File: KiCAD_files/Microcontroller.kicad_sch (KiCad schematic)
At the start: 58 parts, among them J403 RJE721881411, J404 RJE721881411, U401 OwnTech_SPIN, U402 TCAN334GDR, U405 LTC2850xS8, U406 MCP6487T-E/SN

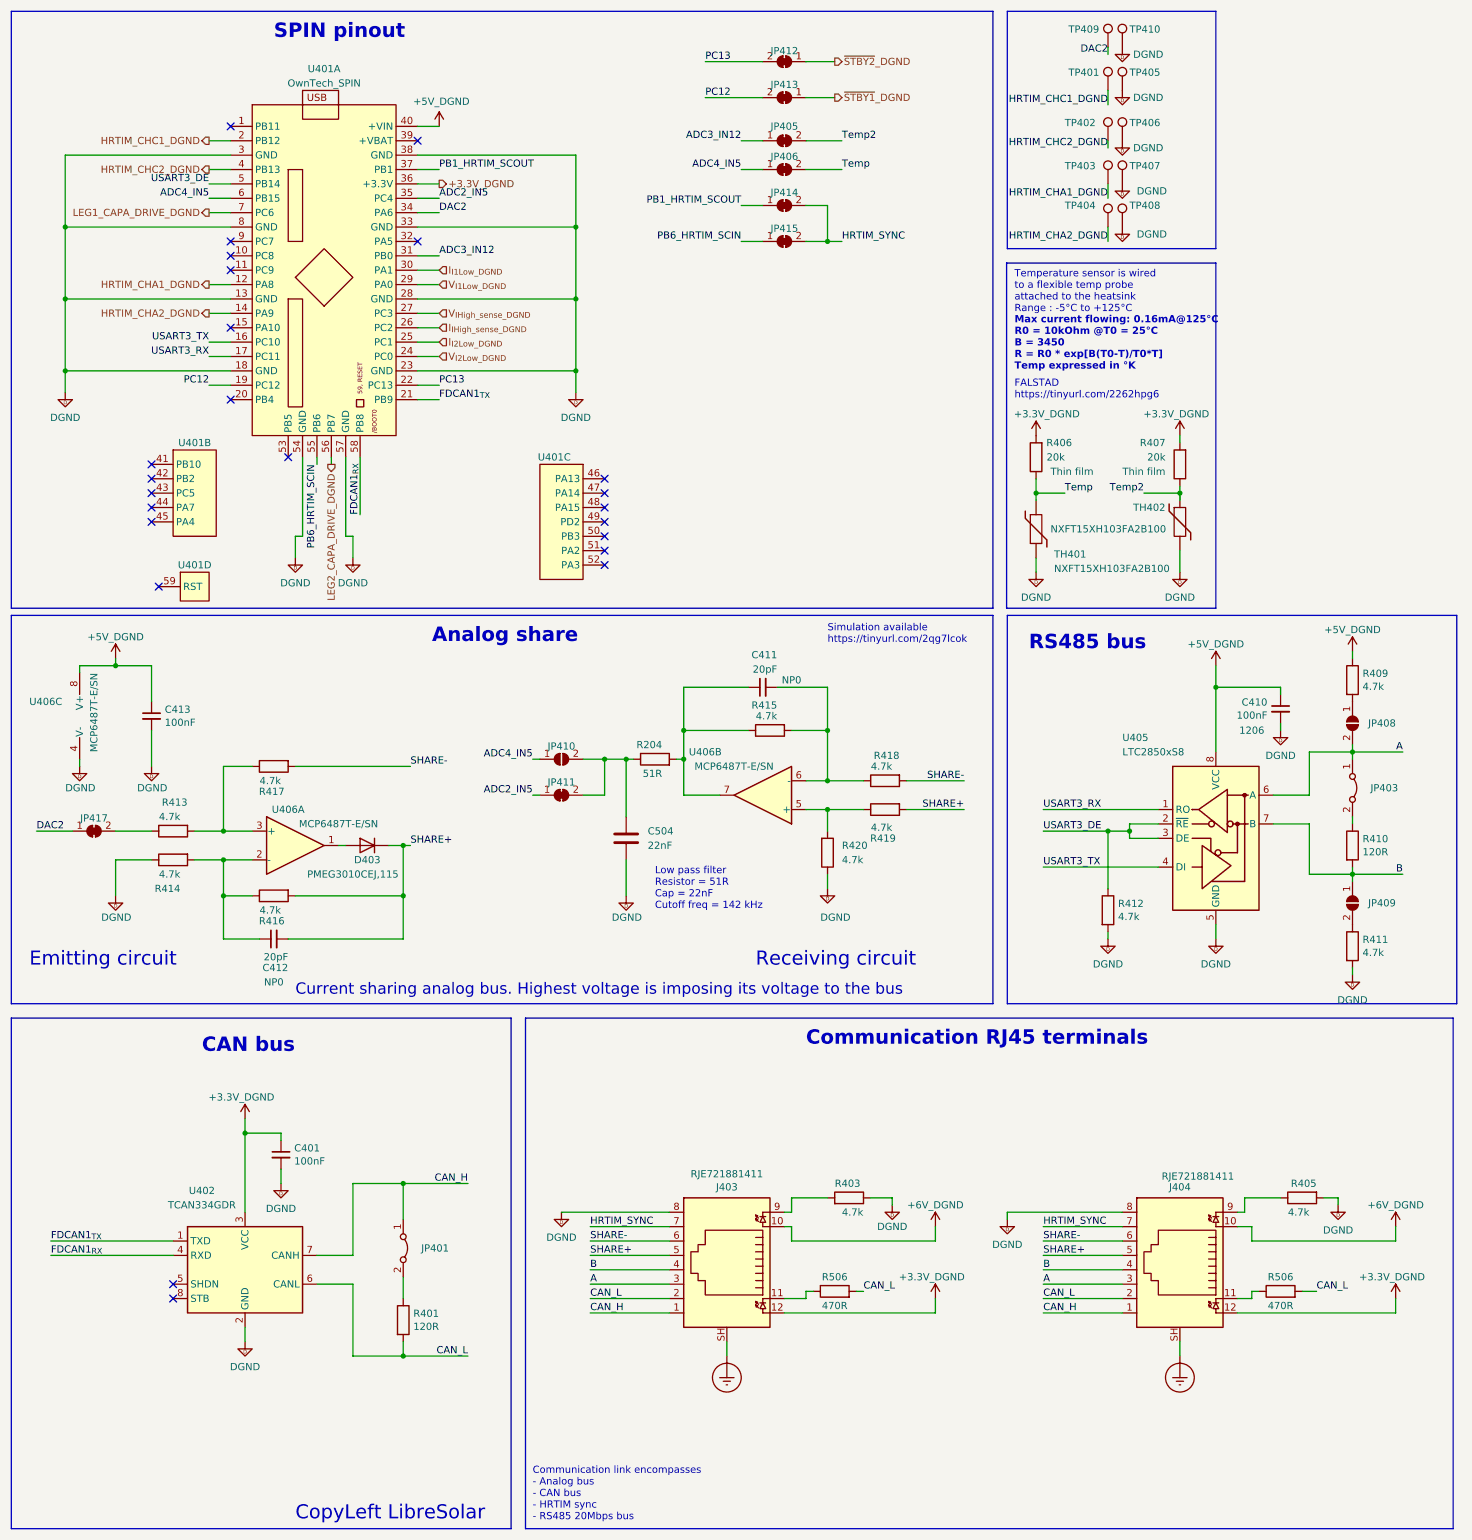
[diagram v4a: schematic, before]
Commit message: Major change - FDCAN1 -> FDCAN2 in order to remove conflit on pin PB8 BOOT0
FDCAN1Rx pin PB8 -> FDCAN2Rx pin PB5
FDCAN1Tx pin PB9 -> FDCAN2Tx pin PB6
HRTIM1_SCIN pin PB6 -> HRTIM1_SCIN pin PB2.

Signed-off-by: Jean Alinei <jean.alinei@laas.fr>
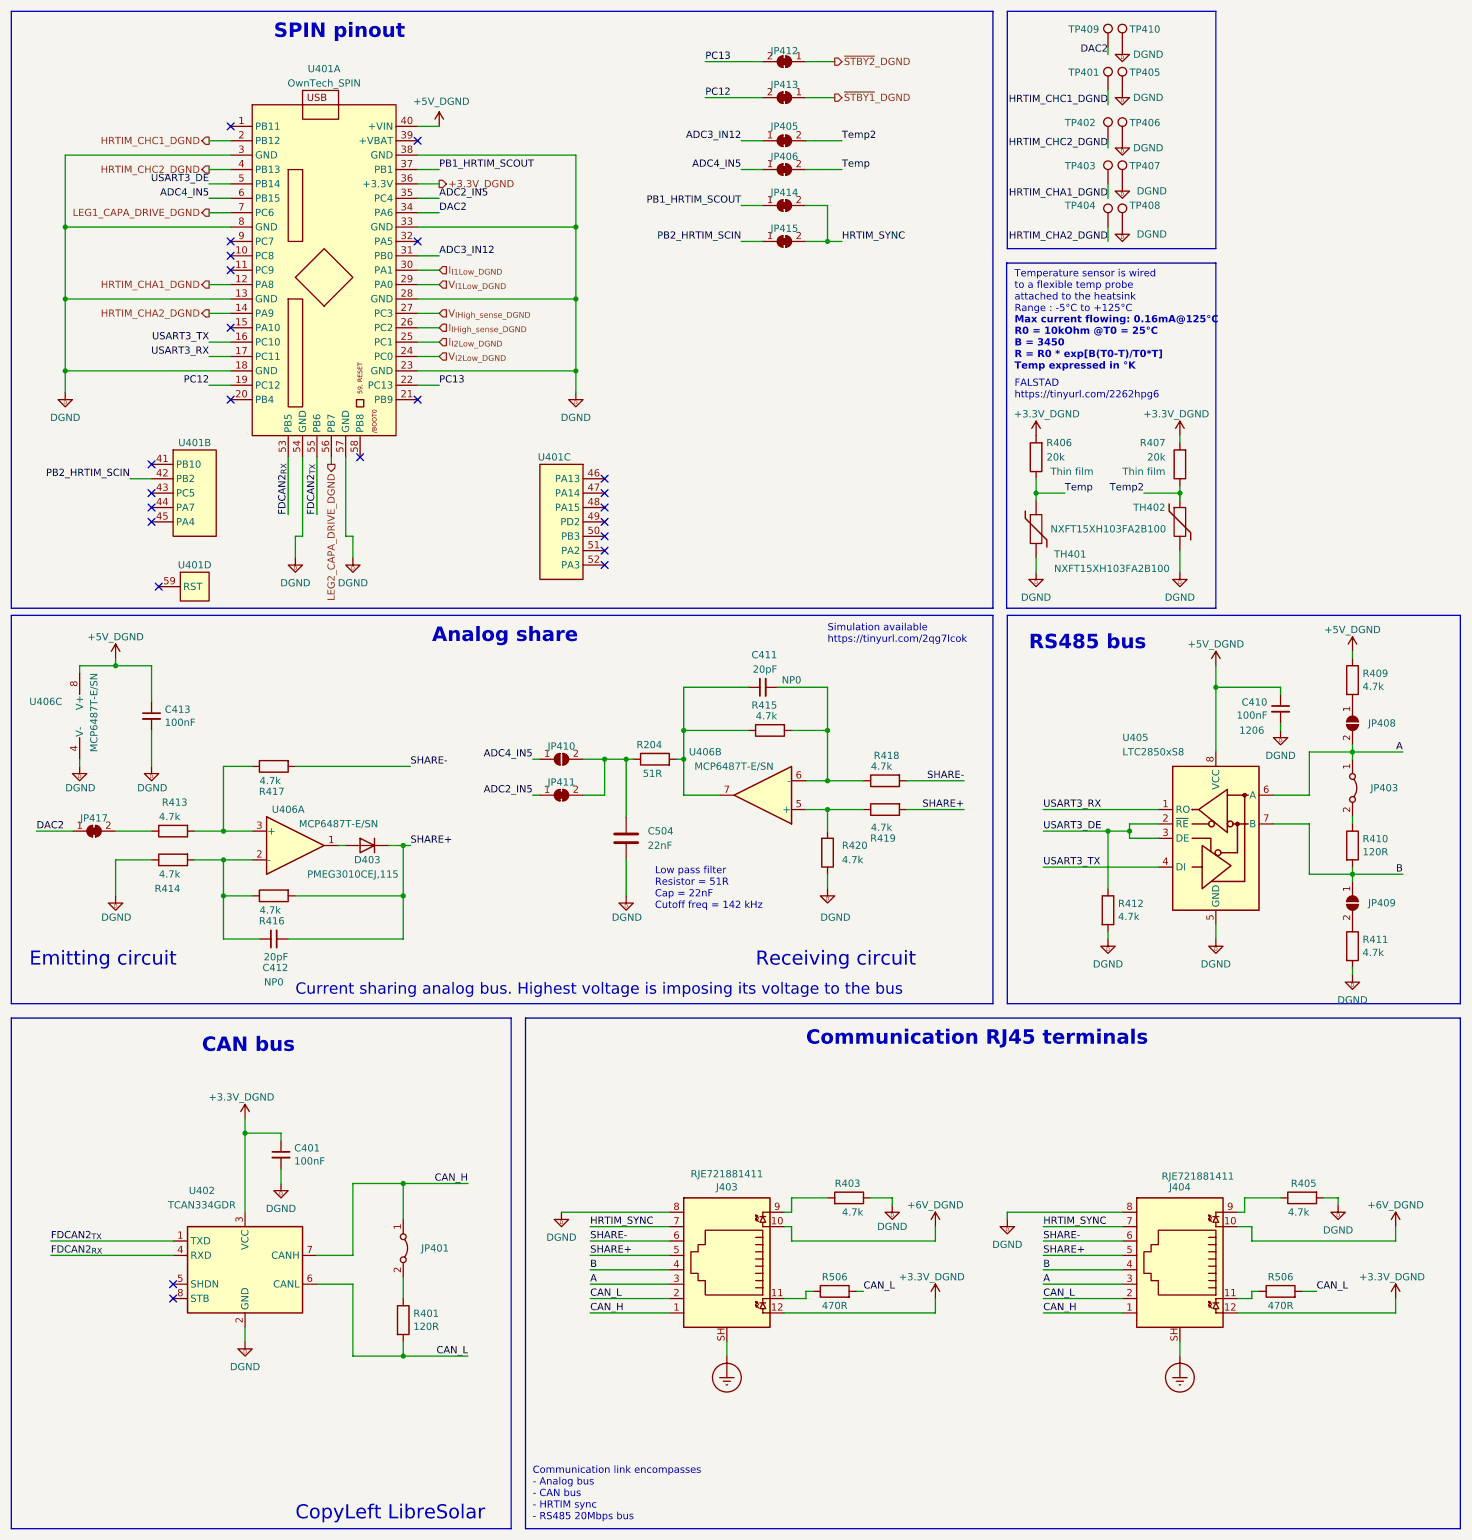
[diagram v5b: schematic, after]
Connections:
- net FDCAN2_{RX}: now reaches U401.53 (PB5)
- net FDCAN2_{RX}: now also U402.4 (RXD)
- net PB2_HRTIM_SCIN: now reaches U401.42 (PB2)
- net PB2_HRTIM_SCIN: now also JP415.1 (A)
- net FDCAN1_{RX}: no longer names the net of U401.58 (PB8)
- net FDCAN1_{RX}: no longer U402.4 (RXD)
- net FDCAN1_{TX}: no longer names the net of U401.21 (PB9)
- net FDCAN1_{TX}: no longer U402.1 (TXD)
- net PB6_HRTIM_SCIN renamed FDCAN2_{TX}
- net FDCAN2_{TX}: now also U402.1 (TXD); no longer JP415.1 (A)
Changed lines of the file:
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@@
   (junction (at 233.68 99.06) (diameter 0) (color 0 0 0 0)
   )
+  (no_connect (at 99.06 82.55))
   (no_connect (at 55.88 238.76))
   (no_connect (at 66.04 59.69))
@@
   (no_connect (at 55.88 241.3))
   (no_connect (at 66.04 82.55))
-  (no_connect (at 76.2 92.71))
   (no_connect (at 52.07 99.06))
   (no_connect (at 52.07 93.98))
-  (no_connect (at 52.07 96.52))
   (no_connect (at 132.08 101.6))
   (no_connect (at 132.08 104.14))
@@
   (no_connect (at 66.04 57.15))
   (no_connect (at 66.04 34.29))
+  (no_connect (at 88.9 92.71))
   (no_connect (at 53.34 115.57))
   (no_connect (at 132.08 111.76))
@@
     (stroke (width 0) (type default))
   )
+  (wire (pts (xy 76.2 92.71) (xy 76.2 102.87))
+    (stroke (width 0) (type default))
+  )
   (wire (pts (xy 52.07 129.54) (xy 45.72 129.54))
     (stroke (width 0) (type default))
@@
     (stroke (width 0) (type default))
   )
-  (wire (pts (xy 81.28 92.71) (xy 81.28 93.98))
-    (stroke (width 0) (type default))
-  )
   (wire (pts (xy 245.11 223.52) (xy 251.46 223.52))
     (stroke (width 0) (type default))
@@
     (stroke (width 0) (type default))
   )
-  (wire (pts (xy 88.9 92.71) (xy 88.9 102.87))
-    (stroke (width 0) (type default))
-  )
   (wire (pts (xy 31.75 158.75) (xy 38.1 158.75))
     (stroke (width 0) (type default))
@@
     (stroke (width 0) (type default))
   )
-  (wire (pts (xy 99.06 82.55) (xy 102.87 82.55))
-    (stroke (width 0) (type default))
-  )
   (wire (pts (xy 132.08 146.05) (xy 132.08 152.4))
     (stroke (width 0) (type default))
@@
     (stroke (width 0) (type default))
   )
+  (wire (pts (xy 48.26 96.52) (xy 52.07 96.52))
+    (stroke (width 0) (type default))
+  )
   (wire (pts (xy 233.68 99.06) (xy 233.68 100.33))
     (stroke (width 0) (type default))
@@
     (stroke (width 0) (type default))
   )
+  (wire (pts (xy 81.28 92.71) (xy 81.28 102.87))
+    (stroke (width 0) (type default))
+  )
   (wire (pts (xy 77.47 106.68) (xy 77.47 110.49))
     (stroke (width 0) (type default))
@@
     (fill (type none))
   )
-  (rectangle (start 203.2 120.65) (end 282.575 189.23)
+  (rectangle (start 203.2 120.65) (end 283.21 189.23)
     (stroke (width 0) (type default))
     (fill (type none))
@@
     (fill (type none))
   )
-  (rectangle (start 118.11 191.77) (end 281.94 281.94)
+  (rectangle (start 118.11 191.77) (end 283.21 281.94)
     (stroke (width 0) (type default))
     (fill (type none))
@@
     (effects (font (size 1.27 1.27)) (justify left bottom))
   )
+  (label "FDCAN2_{RX}" (at 76.2 102.87 90) (fields_autoplaced)
+    (effects (font (size 1.27 1.27)) (justify left bottom))
+  )
   (label "PC12" (at 149.86 29.21 0) (fields_autoplaced)
     (effects (font (size 1.27 1.27)) (justify left bottom))
@@
     (effects (font (size 1.27 1.27)) (justify right bottom))
   )
+  (label "FDCAN2_{TX}" (at 81.28 102.87 90) (fields_autoplaced)
+    (effects (font (size 1.27 1.27)) (justify left bottom))
+  )
   (label "ADC4_IN5" (at 62.23 46.99 180) (fields_autoplaced)
     (effects (font (size 1.27 1.27)) (justify right bottom))
   )
+  (label "PB2_HRTIM_SCIN" (at 48.26 96.52 180) (fields_autoplaced)
+    (effects (font (size 1.27 1.27)) (justify right bottom))
+  )
   (label "Temp2" (at 227.33 99.06 180) (fields_autoplaced)
     (effects (font (size 1.27 1.27)) (justify right bottom))
@@
     (effects (font (size 1.27 1.27)) (justify right bottom))
   )
-  (label "PB6_HRTIM_SCIN" (at 81.28 93.98 270) (fields_autoplaced)
-    (effects (font (size 1.27 1.27)) (justify right bottom))
-  )
   (label "SHARE+" (at 129.54 233.68 0) (fields_autoplaced)
     (effects (font (size 1.27 1.27)) (justify left bottom))
@@
     (effects (font (size 1.27 1.27)) (justify left bottom))
   )
-  (label "FDCAN1_{TX}" (at 34.29 231.14 0) (fields_autoplaced)
+  (label "FDCAN2_{TX}" (at 34.29 231.14 0) (fields_autoplaced)
     (effects (font (size 1.27 1.27)) (justify left bottom))
   )
@@
     (effects (font (size 1.27 1.27)) (justify left bottom))
   )
-  (label "PB6_HRTIM_SCIN" (at 156.21 54.61 180) (fields_autoplaced)
+  (label "PB2_HRTIM_SCIN" (at 156.21 54.61 180) (fields_autoplaced)
     (effects (font (size 1.27 1.27)) (justify right bottom))
   )
@@
     (effects (font (size 1.27 1.27)) (justify left bottom))
   )
-  (label "FDCAN1_{TX}" (at 102.87 82.55 0) (fields_autoplaced)
-    (effects (font (size 1.27 1.27)) (justify left bottom))
-  )
-  (label "FDCAN1_{RX}" (at 34.29 233.68 0) (fields_autoplaced)
+  (label "FDCAN2_{RX}" (at 34.29 233.68 0) (fields_autoplaced)
     (effects (font (size 1.27 1.27)) (justify left bottom))
   )
@@
     (effects (font (size 1.27 1.27)) (justify left bottom))
   )
-  (label "FDCAN1_{RX}" (at 88.9 102.87 90) (fields_autoplaced)
-    (effects (font (size 1.27 1.27)) (justify left bottom))
-  )

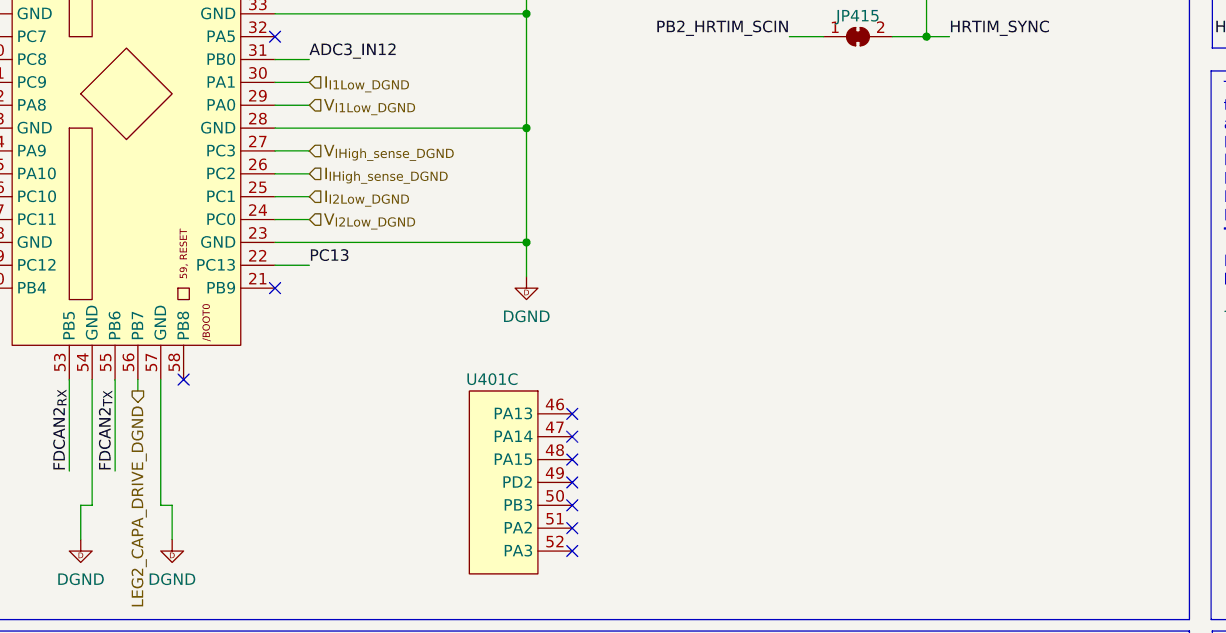
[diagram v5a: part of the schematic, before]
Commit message: Changed the silkscreen to math new CAN pinout - Improved DCDC ground contact Added few missing thermal reliefs - Added few exclusion zones between capacitor terminals
Signed-off-by: Jean Alinei <jean.alinei@laas.fr>
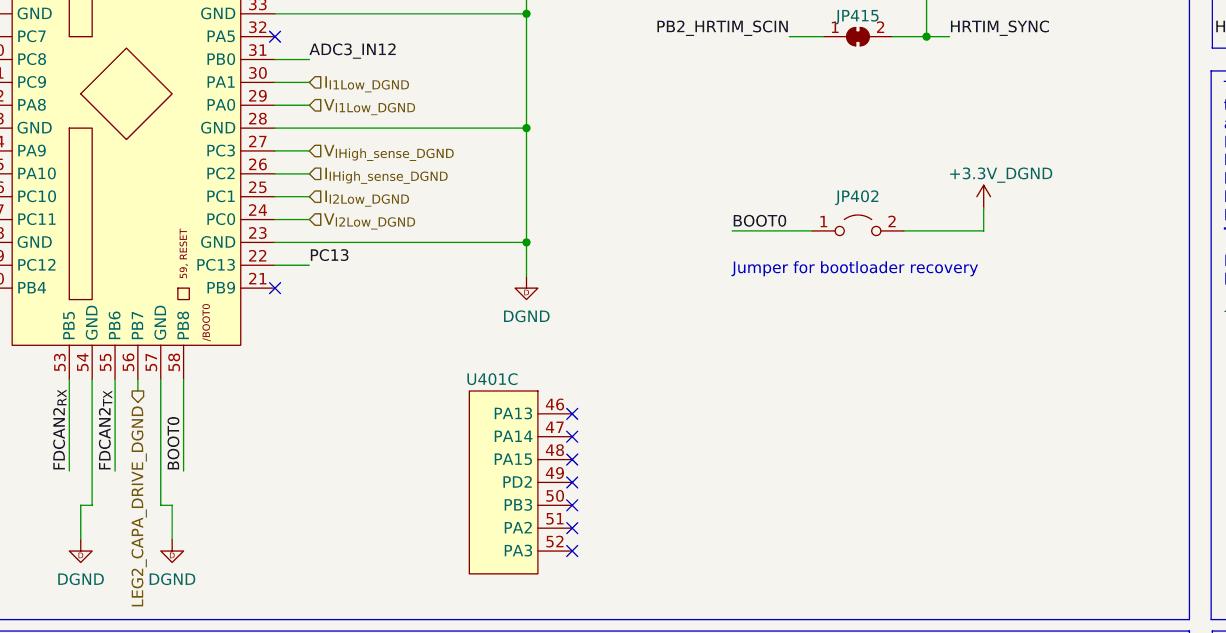
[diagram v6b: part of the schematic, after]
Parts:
- added JP402: Jumper_2_Open, Connector_PinHeader_2.54mm:PinHeader_1x02_P2.54mm_Vertical, symbol Jumper:Jumper_2_Open
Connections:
- net +3.3V_DGND: now also JP402.2 (B)
- net BOOT0: now reaches U401.58 (PB8)
- net BOOT0: now also JP402.1 (A)
- no-connect marks 24 -> 23
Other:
- note added: "Jumper for bootloader recovery"
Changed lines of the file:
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@@
   (no_connect (at 66.04 57.15))
   (no_connect (at 66.04 34.29))
-  (no_connect (at 88.9 92.71))
   (no_connect (at 53.34 115.57))
   (no_connect (at 132.08 111.76))
@@
     (stroke (width 0) (type default))
   )
+  (wire (pts (xy 149.86 76.2) (xy 158.75 76.2))
+    (stroke (width 0) (type default))
+  )
   (wire (pts (xy 45.72 163.83) (xy 45.72 170.18))
     (stroke (width 0) (type default))
@@
     (stroke (width 0) (type default))
   )
+  (wire (pts (xy 177.8 73.66) (xy 177.8 76.2))
+    (stroke (width 0) (type default))
+  )
   (wire (pts (xy 127 64.77) (xy 127 77.47))
     (stroke (width 0) (type default))
@@
     (stroke (width 0) (type default))
   )
+  (wire (pts (xy 88.9 92.71) (xy 88.9 102.87))
+    (stroke (width 0) (type default))
+  )
   (wire (pts (xy 64.77 158.75) (xy 69.85 158.75))
     (stroke (width 0) (type default))
@@
     (stroke (width 0) (type default))
   )
+  (wire (pts (xy 177.8 76.2) (xy 168.91 76.2))
+    (stroke (width 0) (type default))
+  )
   (wire (pts (xy 220.98 27.94) (xy 220.98 30.48))
     (stroke (width 0) (type default))
@@
     (fill (type none))
   )
+  (text "Jumper for bootloader recovery" (at 149.86 81.28 0)
+    (effects (font (size 1.27 1.27)) (justify left bottom))
+  )
   (text "CAN bus" (at 60.96 198.12 0)
     (effects (font (size 2.54 2.54) (thickness 0.508) bold) (justify left bottom))
@@
     (effects (font (size 1.27 1.27)) (justify right bottom))
   )
+  (label "BOOT0" (at 88.9 102.87 90) (fields_autoplaced)
+    (effects (font (size 1.27 1.27)) (justify left bottom))
+  )
   (label "HRTIM_CHC1_DGND" (at 220.98 30.48 180) (fields_autoplaced)
     (effects (font (size 1.27 1.27)) (justify right bottom))
@@
     (effects (font (size 1.27 1.27)) (justify left bottom))
   )
+  (label "BOOT0" (at 149.86 76.2 0) (fields_autoplaced)
+    (effects (font (size 1.27 1.27)) (justify left bottom))
+  )
   (label "SHARE+" (at 195.58 154.94 180) (fields_autoplaced)
     (effects (font (size 1.27 1.27)) (justify right bottom))
@@
     )
   )
+  (symbol (lib_id "Symbols:+3.3V_DGND") (at 177.8 73.66 0) (unit 1)
+    (in_bom no) (on_board no) (dnp no)
+    (property "Reference" "#PWR0403" (at 179.578 73.66 90)
+      (effects (font (size 1.27 1.27)) hide)
+    )
+    (property "Value" "+3.3V_DGND" (at 179.705 69.85 0)
+      (effects (font (size 1.27 1.27)))
+    )
+    (property "Footprint" "" (at 180.975 71.12 0)
+      (effects (font (size 1.27 1.27)) hide)
+    )
+    (property "Datasheet" "" (at 180.975 71.12 0)
+      (effects (font (size 1.27 1.27)) hide)
+    )
+    (pin "1")
+    (instances
+      (project "Power"
+        (path "/8d0c1d66-35ef-4a53-a28f-436a11b54f42/122c01f4-f23e-4db0-9503-7261d96dc78b"
+          (reference "#PWR0403") (unit 1)
+        )
+      )
+    )
+  )
   (symbol (lib_id "Connector:TestPoint") (at 223.52 20.32 0) (unit 1)
     (in_bom yes) (on_board no) (dnp no)
@@
         )
       )
+    )
+  )
+  (symbol (lib_id "Jumper:Jumper_2_Open") (at 163.83 76.2 0) (unit 1)
+    (in_bom yes) (on_board yes) (dnp no)
+    (property "Reference" "JP402" (at 163.83 72.39 0)
+      (effects (font (size 1.27 1.27)))
+    )
+    (property "Value" "Jumper_2_Open" (at 163.83 72.39 0)
+      (effects (font (size 1.27 1.27)) hide)
+    )
+    (property "Footprint" "Connector_PinHeader_2.54mm:PinHeader_1x02_P2.54mm_Vertical" (at 163.83 76.2 0)
+      (effects (font (size 1.27 1.27)) hide)
+    )
+    (property "Datasheet" "~" (at 163.83 76.2 0)
+      (effects (font (size 1.27 1.27)) hide)
+    )
+    (pin "1")
+    (pin "2")
+    (instances
+      (project "Power"
+        (path "/8d0c1d66-35ef-4a53-a28f-436a11b54f42/122c01f4-f23e-4db0-9503-7261d96dc78b"
+          (reference "JP402") (unit 1)
+        )
+      )
